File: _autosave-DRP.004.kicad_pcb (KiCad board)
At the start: 2 copper layers, 53.4 x 26.8 mm, 77 parts, among them J1 Conn_01x03_Pin, J2 USB_C_Receptacle_PowerOnly_6P, J3 Conn_01x03_Pin, J4 Conn_01x05_Pin, J5 Conn_01x03_Pin, J6 Conn_01x03_Pin, Q1 2N7002, Q2 2N7002, Q3 DTC143Z, Q4 2N7002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

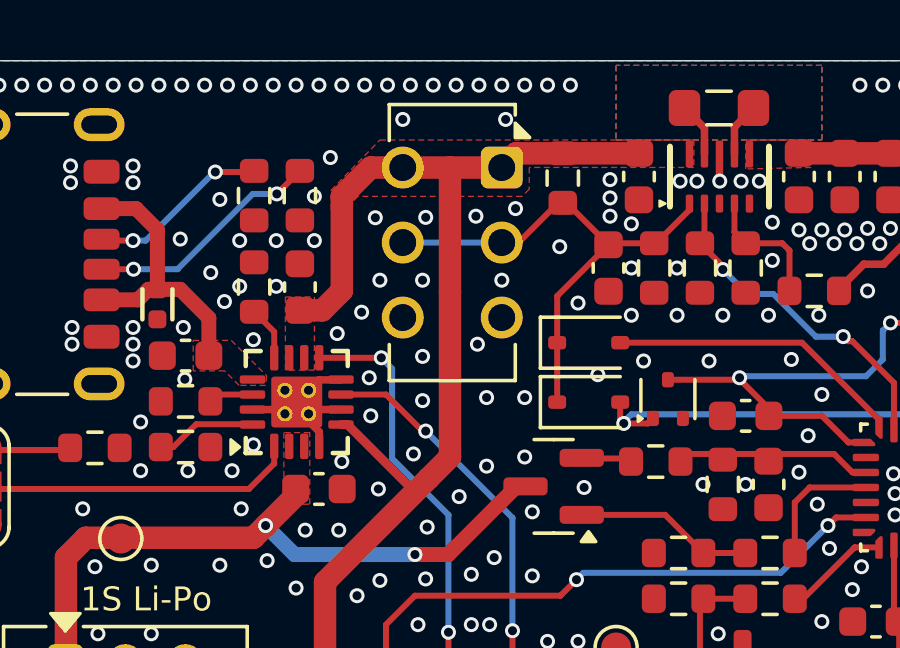
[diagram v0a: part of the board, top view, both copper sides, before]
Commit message: v1 Revision - Better routing - Added testpoints - DUCK - Tweaked drawings
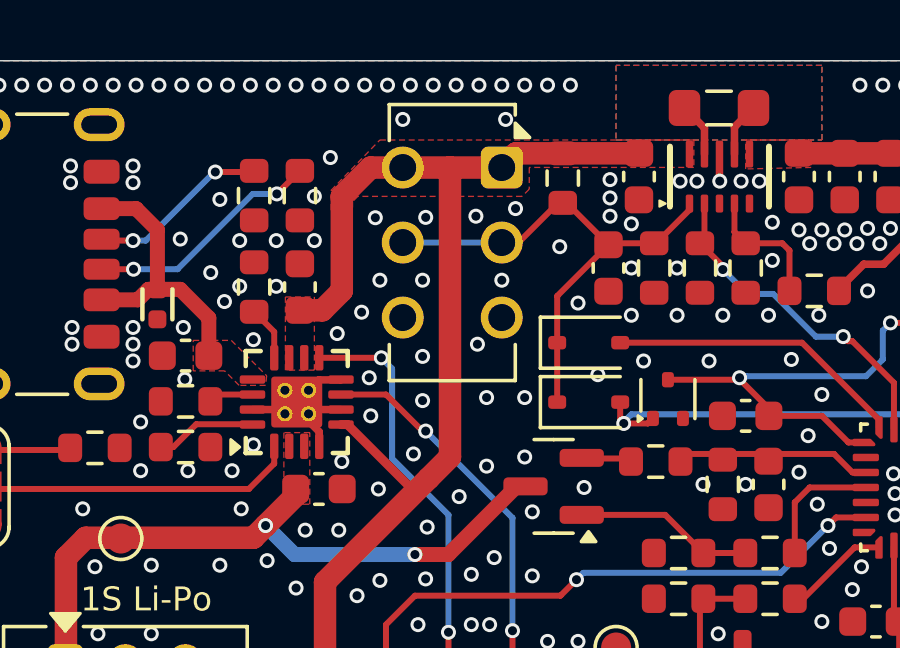
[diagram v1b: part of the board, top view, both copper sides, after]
